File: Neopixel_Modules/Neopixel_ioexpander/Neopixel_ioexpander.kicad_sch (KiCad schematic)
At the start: 15 parts, among them J1 PINHD_1x16_Male, J2 PINHD_1x4_Male, J3 PINHD_1x4_Male, SW2 SW_DIP_x03, U3 MCP23017_ML

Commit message: updated IO expander to bigger MCP23017 footprint
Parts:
- U3: footprint Package_SO:SSOP-28_3.9x9.9mm_P0.635mm -> Package_SO:SOIC-28W_7.5x18.7mm_P1.27mm
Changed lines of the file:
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@@
 			)
 		)
-		(property "Footprint" "Package_SO:SSOP-28_3.9x9.9mm_P0.635mm"
+		(property "Footprint" "Package_SO:SOIC-28W_7.5x18.7mm_P1.27mm"
 			(at 102.87 104.14 0)
 			(effects

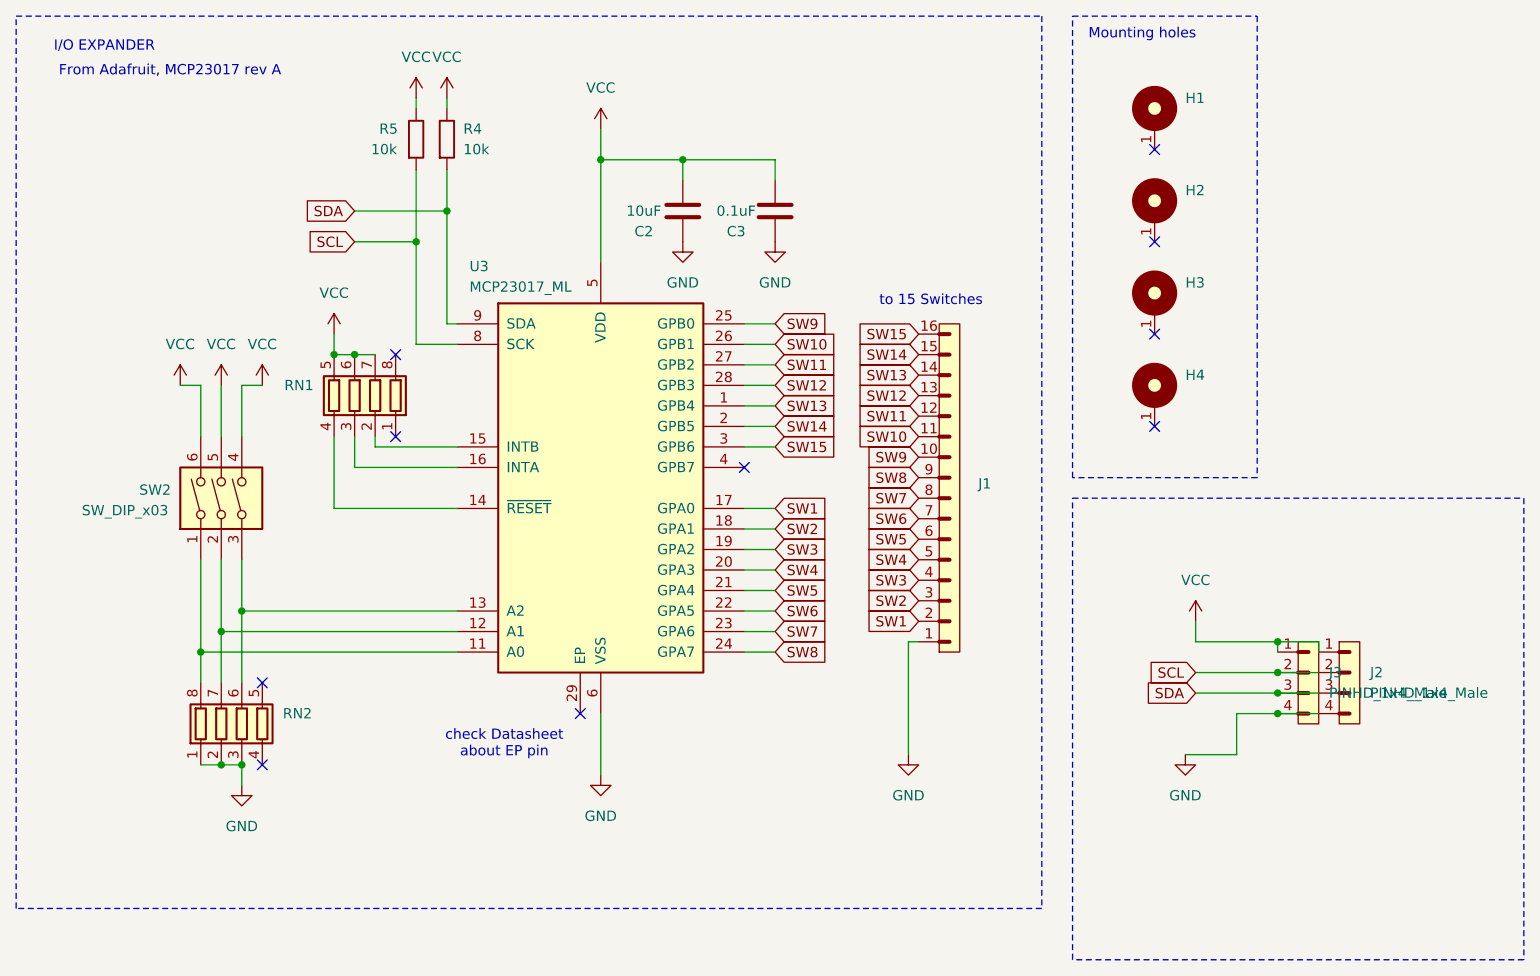
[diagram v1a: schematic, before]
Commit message: PCB Revisions
MCP23017 had incorrect footprints, some tolerances between pads were too tight (shorts), resized some components
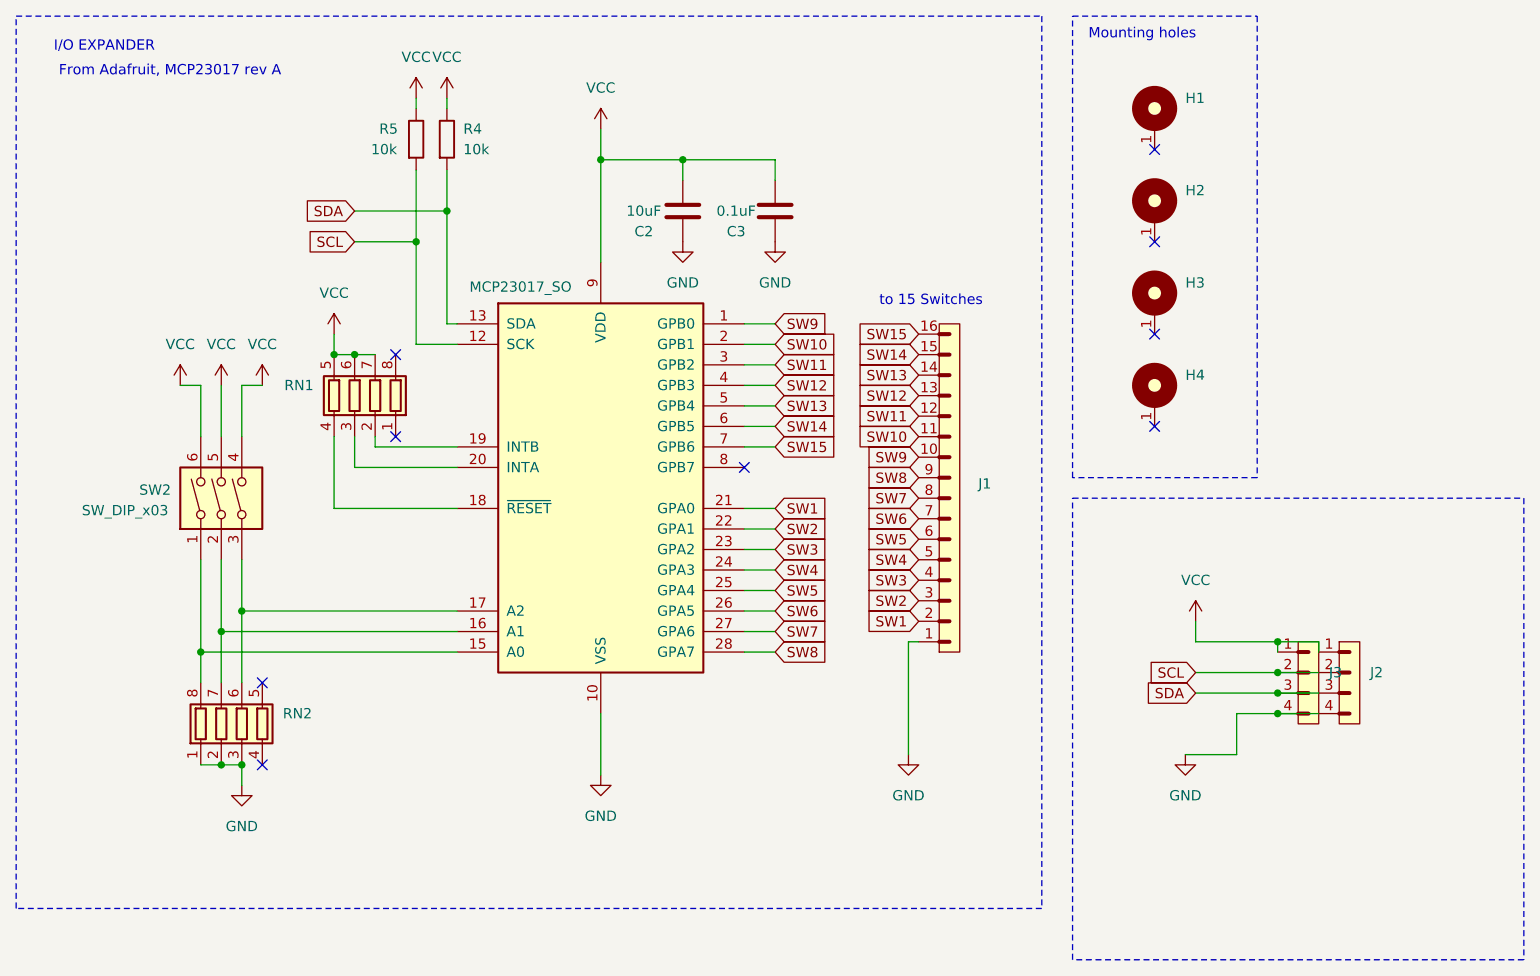
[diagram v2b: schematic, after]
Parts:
- U3: value MCP23017_ML -> MCP23017_SO; footprint Package_SO:SOIC-28W_7.5x18.7mm_P1.27mm -> Package_SO:SOIC-28W_7.5x17.9mm_P1.27mm; symbol Interface_Expansion:MCP23017_ML -> Interface_Expansion:MCP23017_SO
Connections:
- net GND: now also U3.10 (VSS); no longer U3.6 (VSS)
- net SCL: now also U3.12 (SCK); no longer U3.8 (SCK)
- net SDA: now also U3.13 (SDA); no longer U3.9 (SDA)
- net SW1: now also U3.21 (GPA0); no longer U3.17 (GPA0)
- net SW10: now also U3.2 (GPB1); no longer U3.26 (GPB1)
- net SW11: now also U3.3 (GPB2); no longer U3.27 (GPB2)
- net SW12: now also U3.4 (GPB3); no longer U3.28 (GPB3)
- net SW13: now also U3.5 (GPB4); no longer U3.1 (GPB4)
- net SW14: now also U3.6 (GPB5); no longer U3.2 (GPB5)
- net SW15: now also U3.7 (GPB6); no longer U3.3 (GPB6)
- net SW2: now also U3.22 (GPA1); no longer U3.18 (GPA1)
- net SW3: now also U3.23 (GPA2); no longer U3.19 (GPA2)
- net SW4: now also U3.24 (GPA3); no longer U3.20 (GPA3)
- net SW5: now also U3.25 (GPA4); no longer U3.21 (GPA4)
- net SW6: now also U3.26 (GPA5); no longer U3.22 (GPA5)
- net SW7: now also U3.27 (GPA6); no longer U3.23 (GPA6)
- net SW8: now also U3.28 (GPA7); no longer U3.24 (GPA7)
- net SW9: now also U3.1 (GPB0); no longer U3.25 (GPB0)
- net VCC: now also U3.9 (VDD); no longer U3.5 (VDD)
- net at RN1.2 (R2.1): now also U3.19 (INTB); no longer U3.15 (INTB)
- net at RN1.3 (R3.1): now also U3.20 (INTA); no longer U3.16 (INTA)
- net at RN1.4 (R4.1): now also U3.18 (~{RESET}); no longer U3.14 (~{RESET})
- net at RN2.8 (R1.2), SW2.1: now also U3.15 (A0); no longer U3.11 (A0)
- net at RN2.7 (R2.2), SW2.2: now also U3.16 (A1); no longer U3.12 (A1)
- net at RN2.6 (R3.2), SW2.3: now also U3.17 (A2); no longer U3.13 (A2)
- no-connect marks 10 -> 9
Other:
- note removed: "check Datasheet about EP pin"
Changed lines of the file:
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@@
 	)
 	(no_connect
-		(at 95.25 106.68)
-	)
-	(no_connect
 		(at 166.37 59.69)
 	)
@@
 		)
 	)
-	(text "check Datasheet \nabout EP pin"
-		(exclude_from_sim no)
-		(at 85.852 110.49 0)
-		(effects
-			(font
-				(size 1.27 1.27)
-			)
-		)
-	)
 	(text "to 15 Switches"
 		(exclude_from_sim no)
@@
 	)
 	(symbol
-		(lib_id "Interface_Expansion:MCP23017_ML")
+		(lib_id "Interface_Expansion:MCP23017_SO")
 		(at 97.79 78.74 0)
 		(unit 1)
@@
 				)
 				(justify left)
+				(hide yes)
 			)
 		)
-		(property "Value" "MCP23017_ML"
+		(property "Value" "MCP23017_SO"
 			(at 81.534 53.848 0)
 			(effects
@@
 			)
 		)
-		(property "Footprint" "Package_SO:SOIC-28W_7.5x18.7mm_P1.27mm"
+		(property "Footprint" "Package_SO:SOIC-28W_7.5x17.9mm_P1.27mm"
 			(at 102.87 104.14 0)
 			(effects
@@
 			)
 		)
-		(property "Description" "16-bit I/O expander, I2C, interrupts, w pull-ups, QFN-28"
+		(property "Description" "16-bit I/O expander, I2C, interrupts, w pull-ups, SOIC-28"
 			(at 97.79 78.74 0)
 			(effects
@@
 		(pin "22"
 		)
-		(pin "29"
-		)
 		(pin "3"
 		)
@@
 				)
 				(justify left)
+				(hide yes)
 			)
 		)
@@
 				)
 				(justify left)
+				(hide yes)
 			)
 		)
